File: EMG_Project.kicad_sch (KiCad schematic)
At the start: 29 parts, among them J1 Conn_01x04, J2 AudioJack3, U1 CJ432, U2 AMPLIFIER-INA331DGK_MSOP8, U3 OPA333AIDBVR

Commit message: First version of the Sensor complete
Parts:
- removed J1: Conn_01x04, symbol Connector_Generic:Conn_01x04
- added C11, C12, C13: 1u, symbol Device:C
- added J1: Conn_01x02, symbol Connector_Generic:Conn_01x02
- added J10, J11, J12, J13, J14, J15, J16, J3, J4, J5, J6, J7, J8, J9: Conn_01x01, symbol Connector_Generic:Conn_01x01
- added R14, R17: 100k, symbol Device:R
- added R15: 1m, symbol Device:R
- added R16, R19: 0, symbol Device:R
- added R18: 1k, symbol Device:R
- added R20: 10k, symbol Device:R
- added U4: OPA333AIDBVR, OPA333AIDBVR:SOT95P280X145-5N, symbol OPA333AIDBVR:OPA333AIDBVR
- C10, C9: value 0.1u -> 100n
- R12, R13: value R -> 10k
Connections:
- net GND: now also U3.2 (V-), J1.1 (Pin_1), J16.1 (Pin_1), J3.1 (Pin_1), J4.1 (Pin_1), J5.1 (Pin_1), J6.1 (Pin_1), J7.1 (Pin_1), J8.1 (Pin_1), R20.2, U4.2 (V-)
- net VCC: now also U3.5 (V+), J1.2 (Pin_2), J12.1 (Pin_1), U4.5 (V+)
- net V_REF: now also U3.3 (+IN), J11.1 (Pin_1), R15.2, R19.2
- net at R12.1, U2.5 (REF): now also U3.1 (OUT), C11.1
- net at U3.4 (-IN): now also C11.2, R14.1
- net V_OUT_INST: now reaches R13.1, U2.6 (VOUT)
- net V_OUT_INST: now also C12.1, J13.1 (Pin_1), R14.2
- net INST_IN_N renamed INST_INST_N
- net INST_INST_N: now also J9.1 (Pin_1)
- net INST_IN_P renamed INST_INST_P
- net INST_INST_P: now also J10.1 (Pin_1)
- new net: R18.2, R19.1
- new net: C13.2, R17.1, R18.1, U4.4 (-IN)
- new net: C12.2, R15.1, R16.2
- new net V_OUT_HP: J14.1 (Pin_1), R16.1, U4.3 (+IN)
- new net V_OUT_SENSOR: C13.1, J15.1 (Pin_1), R17.2, R20.1, U4.1 (OUT)
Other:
- note added: "High Frequency Rejeection"
- note added: "High-Pass Filter"
- note added: "Power LED"
- note added: "Voltage Reference"
- moved on the sheet: C1, C10, C2, C3, C4, C5, C6, C7, C8, C9, D1, J2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

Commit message: Added ATtiny
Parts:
- removed J3: Conn_01x01, symbol Connector_Generic:Conn_01x01
- added C14, C16: 100n, symbol Device:C
- added D2: LED, symbol Device:LED
- added J17: Conn_01x04, symbol Connector_Generic:Conn_01x04
- added J18: Conn_01x01, symbol Connector_Generic:Conn_01x01
- added R21: 10k, symbol Device:R
- added R22: 400, symbol Device:R
- added SW1: SW_SPST, symbol Switch:SW_SPST
- added U5: ATTINY13-20SSU, S8S1_ATM, symbol ATTINY13-20SSU:ATTINY13-20SSU
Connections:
- net GND: now also J1.2 (Pin_2), C14.2, C16.2, D2.1 (K), J18.1 (Pin_1), SW1.2 (B), U5.4 (GND); no longer J1.1 (Pin_1)
- net VCC: now also J1.1 (Pin_1); no longer J1.2 (Pin_2)
- net V_OUT_SENSOR: now also U5.2 (PB3)
- new net: D2.2 (A), R22.2
- new net +3.3V: C16.1, R21.2, U5.8 (VCC)
- new net MISO: J17.2 (Pin_2), U5.6 (PB1)
- new net MOSI: J17.3 (Pin_3), U5.5 (PB0)
- new net RST: C14.1, J17.4 (Pin_4), R21.1, SW1.1 (A), U5.1 (PB5)
- new net SCK: J17.1 (Pin_1), U5.7 (PB2)
- new net TEST_LED: R22.1, U5.3 (PB4)
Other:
- note added: "Reset Pushbutton"
- note removed: "Inst"
- note removed: "OPAMP"
- moved on the sheet: C10, C11, C4, C5, C6, C7, C8, C9, J1, J10, J11, J12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

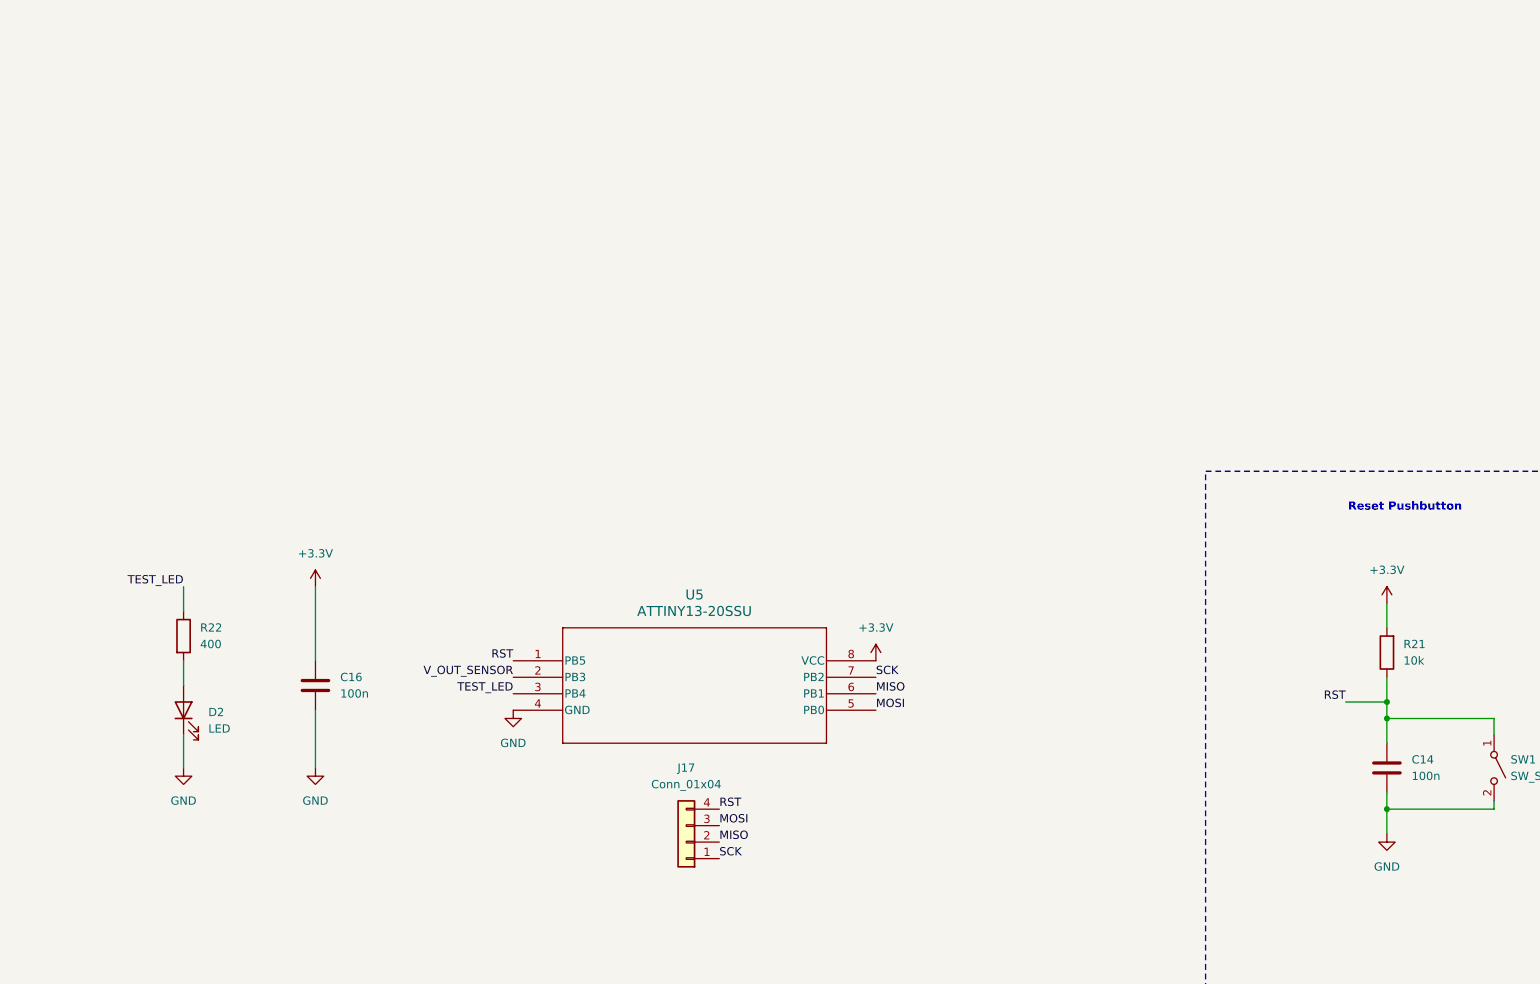
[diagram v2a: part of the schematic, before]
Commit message: Rearrangeed the footprints and symbols
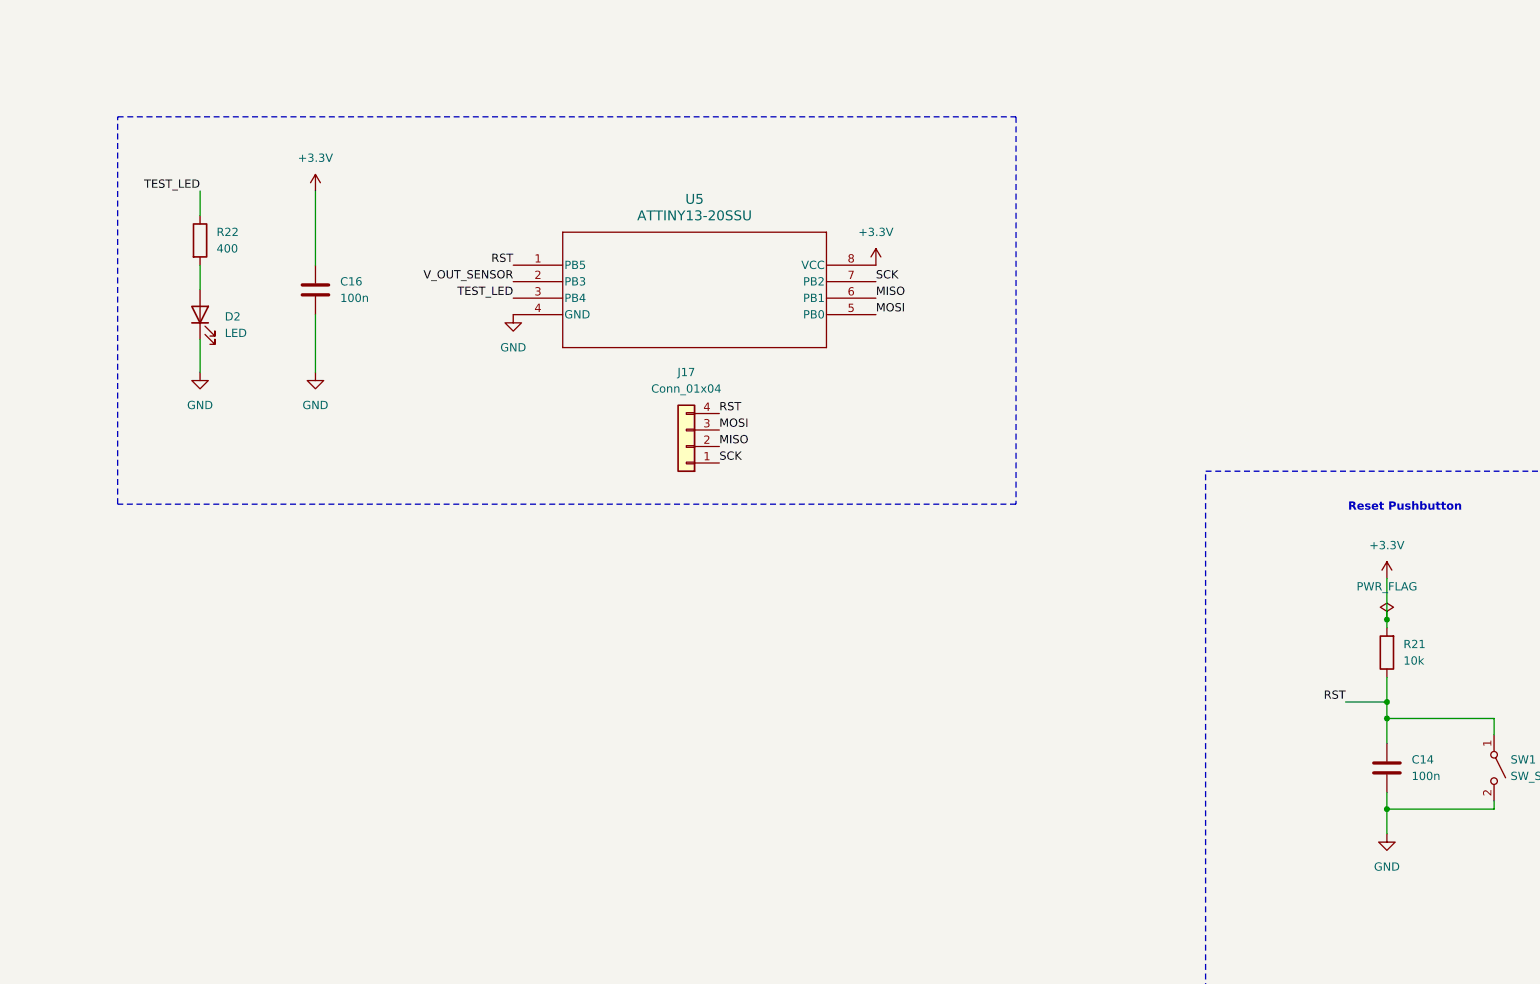
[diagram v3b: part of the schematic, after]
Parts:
- removed U2: AMPLIFIER-INA331DGK_MSOP8, AMPLIFIER-INA331DGK_MSOP8_:SOP65P490X110-8N, symbol INA331IDGKT:AMPLIFIER-INA331DGK_MSOP8_
- added U2: AMPLIFIER-INA331DGK_MSOP8, EMG Projct Footprints:SOP65P490X110-8N, symbol AMPLIFIER-INA331DGK_MSOP8_:AMPLIFIER-INA331DGK_MSOP8_
- U3, U4: footprint OPA333AIDBVR:SOT95P280X145-5N -> EMG Projct Footprints:SOT95P280X145-5N
- U5: footprint S8S1_ATM -> EMG Projct Footprints:S8S1_ATM
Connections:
- net GND: now also U2.4 (V-)
- net INST_INST_N: now also U2.2 (VIN-)
- net INST_INST_P: now also U2.3 (VIN+)
- net VCC: now also U2.7 (V+), U2.8 (SHUTDOWN)
- net V_OUT_INST: now also U2.6 (VOUT)
- net at C11.1, R12.1, U3.1 (OUT): now also U2.5 (REF)
- net at R12.2, R13.2: now also U2.1 (RG)
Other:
- moved on the sheet: C16, D2, J17, R22

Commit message: First version of the whole schematic
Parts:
- removed J1: Conn_01x02, symbol Connector_Generic:Conn_01x02
- removed J17: Conn_01x04, symbol Connector_Generic:Conn_01x04
- added C15: 22uF, symbol Device:C
- added C18: 1u, symbol Device:C
- added C20: 0.1u, symbol Device:C
- added C21: 22u, symbol Device:C
- added J1: Conn_01x03, symbol Connector_Generic:Conn_01x03
- added J3: Conn_01x06, symbol Connector_Generic:Conn_01x06
- added L1: 3.3u, symbol Device:L
- added R23: 100k, symbol Device:R
- added R24: 976k, symbol Device:R
- added R25: 220k, symbol Device:R
- added U6: MP2322GQH-Z, MP2322GQHZ, symbol MP2322GQH-Z:MP2322GQH-Z
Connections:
- net VCC is gone; now on net +3.3V: C1.1, C10.1, C7.1, C8.1, C9.1, J12.1 (Pin_1), R1.1, R4.1, U2.7 (V+), U2.8 (SHUTDOWN), U3.5 (V+), U4.5 (V+)
- net +3.3V: now also J1.2 (Pin_2), R23.1
- net GND: now also C15.2, C18.2, C21.2, J3.4 (Pin_4), R25.2, U6.1 (GND)
- net MISO: now also J3.3 (Pin_3)
- net MOSI: now also J3.5 (Pin_5)
- net RST: now also J3.1 (Pin_1)
- net SCK: now also J3.2 (Pin_2)
- new net: C18.1, U6.4 (VCC)
- new net: C21.1, L1.2, R24.1
- new net: C20.2, L1.1
- new net: R24.2, R25.1
- new net +5V: C15.1, J1.3 (Pin_3), J3.6 (Pin_6), U6.2 (IN), U6.3 (EN)
- new net REG_OUT: J1.1 (Pin_1)
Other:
- note added: "ATTINY 13"
- note added: "V_REF = 1.24V*(1 + R2/R3)"
- note added: "Volatge Regulator"
- moved on the sheet: C1, C14, C16, D1, D2, R1, R21, R22, SW1, U5

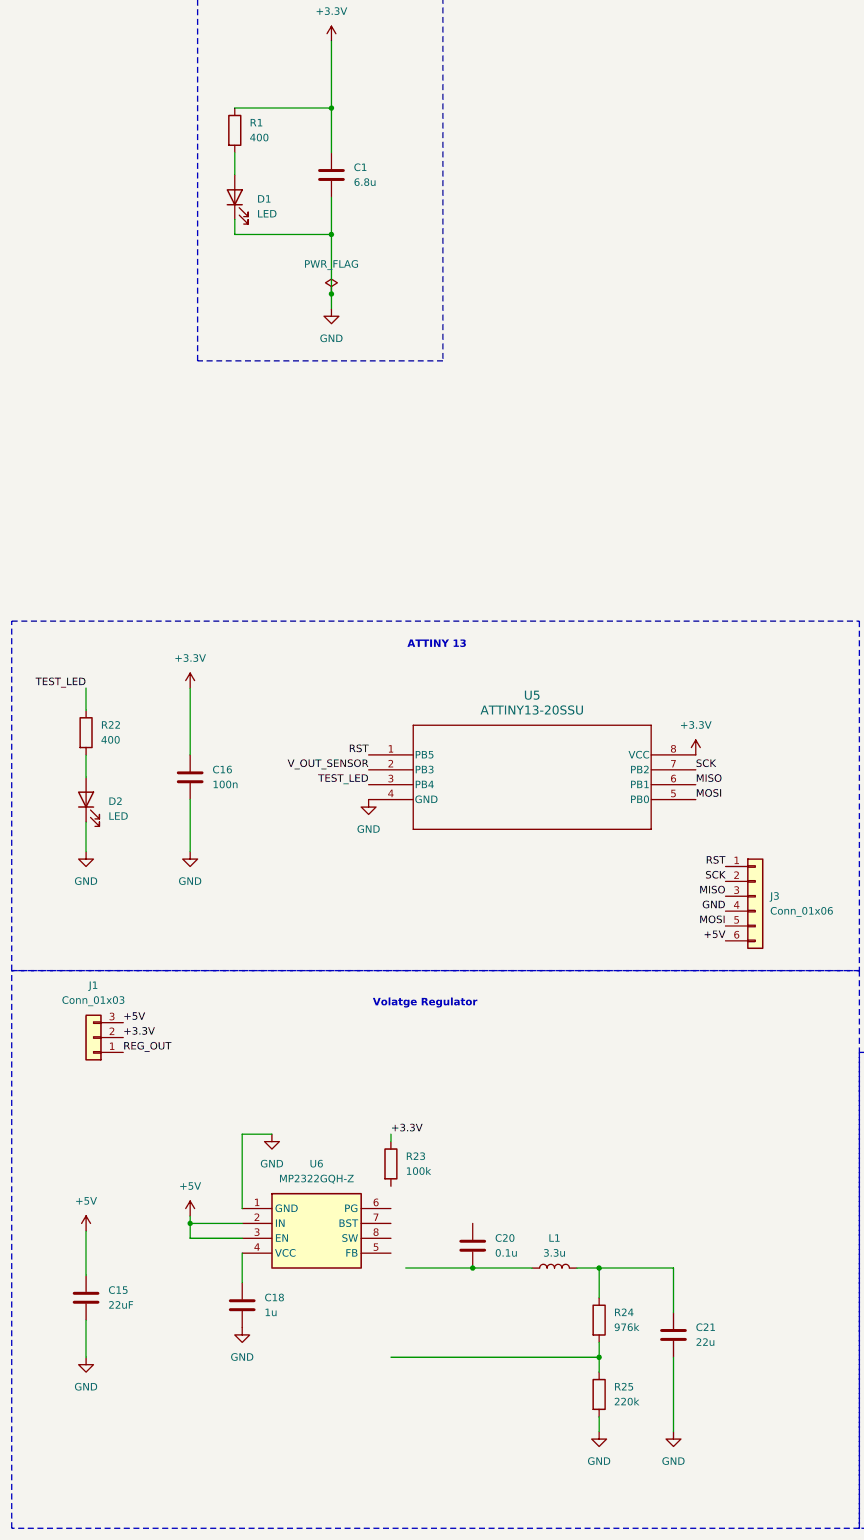
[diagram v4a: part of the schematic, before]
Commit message: Made Changes to the voltage regulator
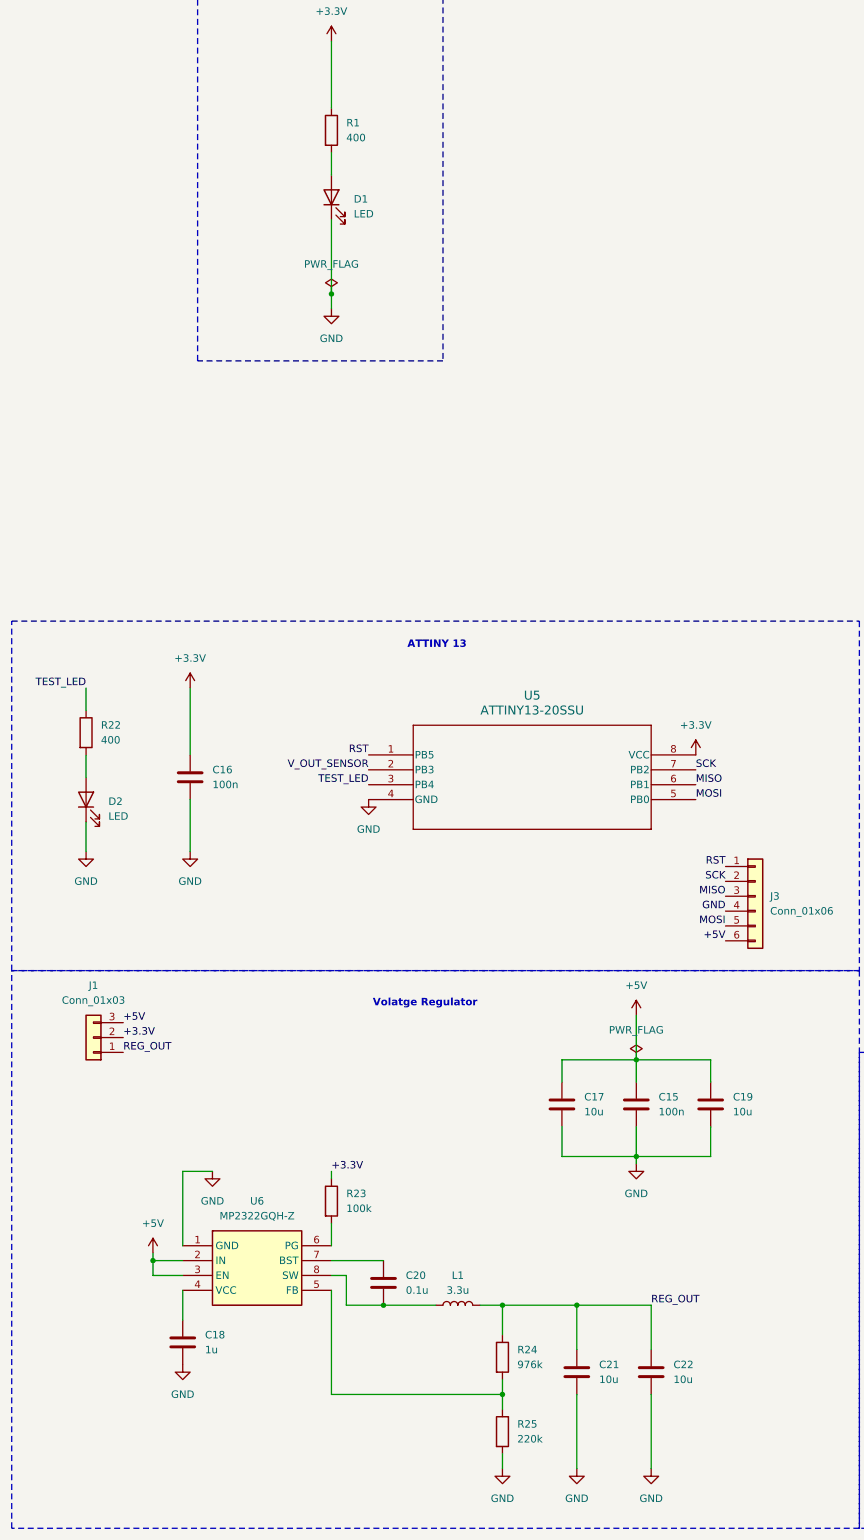
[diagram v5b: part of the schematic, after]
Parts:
- removed C1: 6.8u, symbol Device:C
- added C17, C19, C22: 10u, symbol Device:C
- C15: value 22uF -> 100n
- C21: value 22u -> 10u
- U6: footprint MP2322GQHZ -> EMG Projct Footprints:MP2322GQHZ
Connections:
- net +5V: now also C17.1, C19.1
- net GND: now also C17.2, C19.2, C22.2
- net REG_OUT: now also C21.1, L1.2, R24.1, C22.1
- net at R23.2: now also U6.6 (PG)
- net at C20.1: now also U6.7 (BST)
- net at C20.2, L1.1: now also U6.8 (SW)
- net at R24.2, R25.1: now also U6.5 (FB)
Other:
- moved on the sheet: C15, C18, C20, D1, L1, R1, R23, R24, R25, U6
